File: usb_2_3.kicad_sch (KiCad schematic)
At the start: 0 parts

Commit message: Finished the schematic capture for the USb 2.0/3.0
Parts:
- added C26, C27, C28, C29: 100NF/50V, A_HDJ_Library:C_0402_1005Metric, symbol Device:C_Small
- added C30, C31, C32: 22mF/10V, A_HDJ_Library:C_0603_1608Metric, symbol Device:C
- added D5, D6, D7, D8: ESD9B5.0ST5G, A_HDJ_Library:D_0402_1005Metric, symbol Diode:ESD9B5.0ST5G
- added F2, F3, F4, F5: 6V/1A, A_HDJ_Library:Fuse_0805_2012Metric, symbol Device:Fuse
- added J4: USB3_A_Stacked, A_HDJ_Library:USB3_A_Molex_48406-0001_Horizontal_Stacked, symbol Connector:USB3_A_Stacked
- added J4B: USB3_A_Stacked, symbol Connector:USB3_A_Stacked
- added J5: USB_A_Stacked, A_HDJ_Library:USB_A_CUI_UJ2-ADH-TH_Horizontal_Stacked, symbol Connector:USB_A_Stacked
- added U3, U4, U5: D3V3XA4B10LP, A_HDJ_Library:Diodes_UDFN-10_1.0x2.5mm_P0.5mm, symbol Power_Protection:D3V3XA4B10LP
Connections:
- new net: F3.2, J5.5 (VBUS2)
- new net: F2.2, J5.1 (VBUS1)
- new net: F5.2, J4B.10 (VBUS2)
- new net: F4.2, J4.1 (VBUS1)
- new net +5V: C30.2, C31.2, C32.2, F2.1, F3.1, F4.1, F5.1
- new net CON_USB3_SSTX_N: C26.2, C28.2, J4.8 (SSTX1-), J4B.17 (SSTX2-)
- new net CON_USB3_SSTX_P: C27.2, C29.2, J4.9 (SSTX1+), J4B.18 (SSTX2+)
- new net GND: C30.1, C31.1, C32.1, D5.2 (A2), D6.2 (A2), D7.2 (A2), D8.2 (A2), J4.4 (GND1), J4.7 (DRAIN1), J4.SH (SHIELD), J4B.13 (GND2), J4B.16 (DRAIN2), J4B.SH (SHIELD), J5.4 (GND1), J5.8 (GND2), J5.SH (Shield), U3.3 (VSS), U3.8 (VSS), U4.3 (VSS), U4.8 (VSS), U5.3 (VSS), U5.8 (VSS)
- new net USB3_SSRT_N: C26.1, U3.5, U3.6 (NC)
- new net USB3_SSRT_P: C27.1, U3.4, U3.7 (NC)
- new net USB3_SSRX_N: J4.5 (SSRX1-), J4B.14 (SSRX2-), U5.1, U5.10 (NC), U5.5, U5.6 (NC)
- new net USB3_SSRX_P: J4.6 (SSRX1+), J4B.15 (SSRX2+), U5.2, U5.4, U5.7 (NC), U5.9 (NC)
- new net USB4_SSRT_N: C28.1, U3.1, U3.10 (NC)
- new net USB4_SSRT_P: C29.1, U3.2, U3.9 (NC)
- new net USB_2_P1+: J4.3 (D1+), J4B.12 (D2+)
- new net USB_2_P1-: J4.2 (D1-), J4B.11 (D2-)
- new net USB_2_P3+: D7.1 (A1), J5.7 (D2+), U4.4, U4.7 (NC)
- new net USB_2_P3-: D8.1 (A1), J5.6 (D2-), U4.5, U4.6 (NC)
- new net USB_2_P5+: D5.1 (A1), J5.3 (D1+), U4.1, U4.10 (NC)
- new net USB_2_P5-: D6.1 (A1), J5.2 (D1-), U4.2, U4.9 (NC)

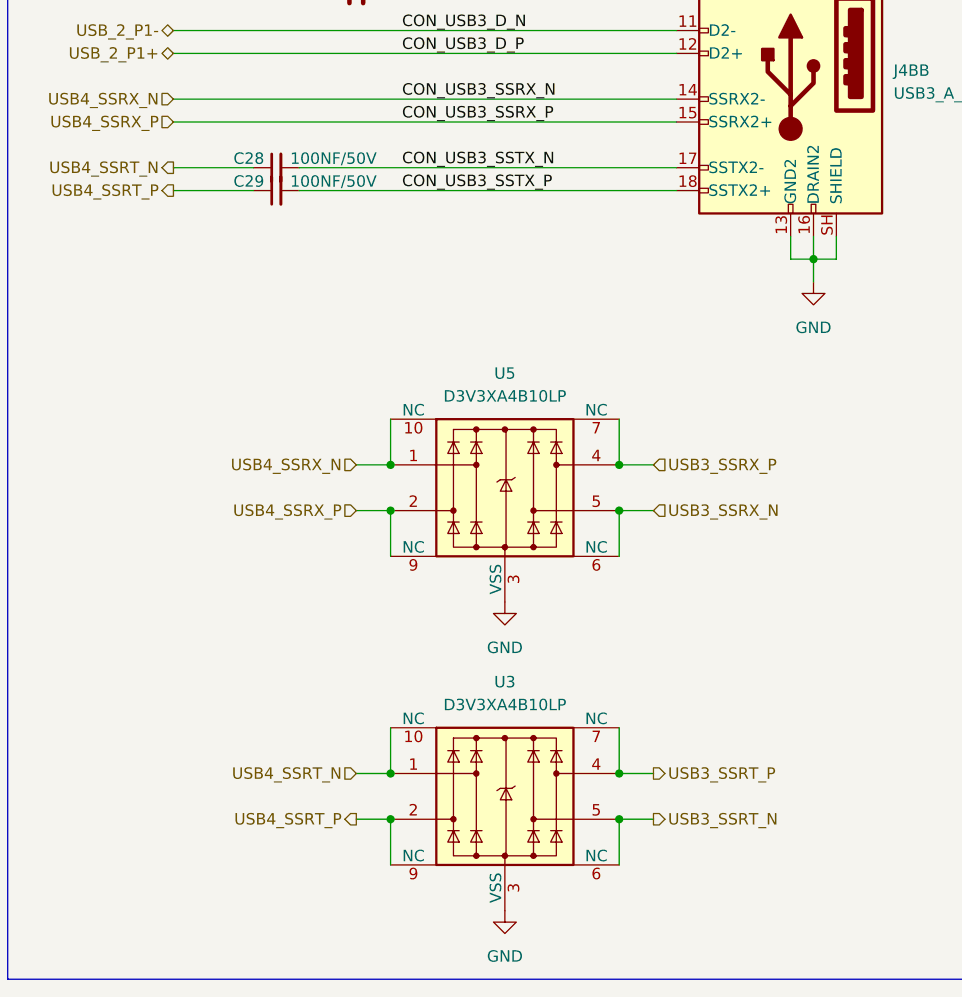
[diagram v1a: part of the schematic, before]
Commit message: Fixed the labels to the netlabels in the USB schema sheet
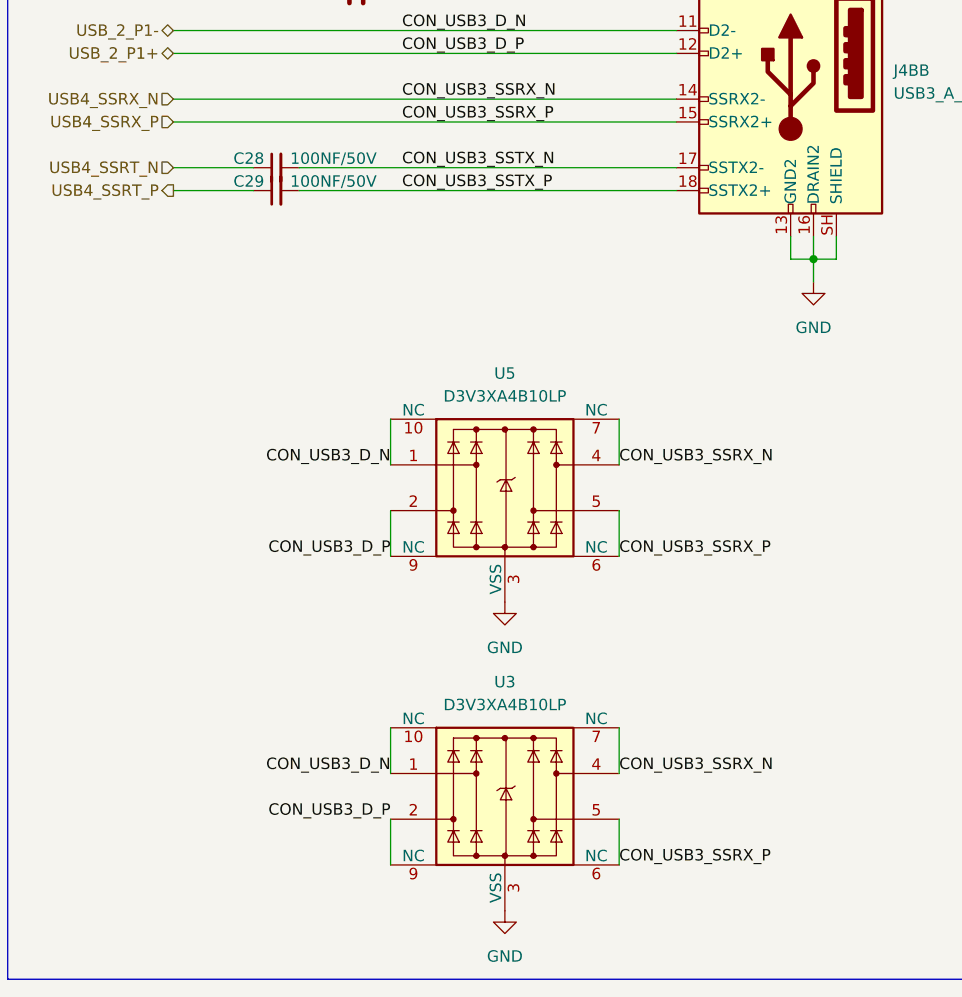
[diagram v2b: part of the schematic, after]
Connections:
- net USB3_SSRT_N: no longer U3.5, U3.6 (NC)
- net USB3_SSRT_P: no longer U3.4, U3.7 (NC)
- net USB3_SSRX_N: now also U3.4, U3.7 (NC), U5.4, U5.7 (NC); no longer U5.1, U5.10 (NC), U5.5, U5.6 (NC)
- net USB3_SSRX_P: now also U3.5, U3.6 (NC), U5.5, U5.6 (NC); no longer U5.2, U5.4, U5.7 (NC), U5.9 (NC)
- net USB4_SSRT_N: no longer U3.1, U3.10 (NC)
- net USB4_SSRT_P: no longer U3.2, U3.9 (NC)
- net USB_2_P1+: now also U3.2, U3.9 (NC), U5.2, U5.9 (NC)
- net USB_2_P1-: now also U3.1, U3.10 (NC), U5.1, U5.10 (NC)
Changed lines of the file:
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@@
-	)
-	(junction
-		(at 55.88 133.35)
-		(diameter 0)
-		(color 0 0 0 0)
-	)
-	(junction
-		(at 55.88 138.43)
-		(diameter 0)
-		(color 0 0 0 0)
-	)
-	(junction
-		(at 81.28 172.72)
-		(diameter 0)
-		(color 0 0 0 0)
 	)
 	(junction
@@
 	)
 	(junction
-		(at 55.88 172.72)
-		(diameter 0)
-		(color 0 0 0 0)
-	)
-	(junction
 		(at 210.82 129.54)
 		(diameter 0)
@@
 	)
 	(junction
-		(at 55.88 167.64)
-		(diameter 0)
-		(color 0 0 0 0)
-	)
-	(junction
-		(at 81.28 133.35)
-		(diameter 0)
-		(color 0 0 0 0)
-	)
-	(junction
 		(at 102.87 59.69)
 		(diameter 0)
 		(color 0 0 0 0)
 	)
-	(junction
-		(at 81.28 138.43)
-		(diameter 0)
-		(color 0 0 0 0)
-	)
-	(junction
-		(at 81.28 167.64)
-		(diameter 0)
-		(color 0 0 0 0)
-	)
 	(wire
 		(pts
@@
 	(wire
 		(pts
-			(xy 81.28 133.35) (xy 85.09 133.35)
-		)
-		(stroke
-			(width 0)
-			(type default)
-		)
-	)
-	(wire
-		(pts
-			(xy 52.07 167.64) (xy 55.88 167.64)
-		)
-		(stroke
-			(width 0)
-			(type default)
-		)
-	)
-	(wire
-		(pts
 			(xy 45.72 102.87) (xy 87.63 102.87)
 		)
@@
 	(wire
 		(pts
-			(xy 81.28 172.72) (xy 85.09 172.72)
-		)
-		(stroke
-			(width 0)
-			(type default)
-		)
-	)
-	(wire
-		(pts
 			(xy 31.75 44.45) (xy 87.63 44.45)
 		)
@@
 	(wire
 		(pts
-			(xy 52.07 138.43) (xy 55.88 138.43)
-		)
-		(stroke
-			(width 0)
-			(type default)
-		)
-	)
-	(wire
-		(pts
 			(xy 194.31 134.62) (xy 210.82 134.62)
 		)
@@
 	(wire
 		(pts
-			(xy 52.07 133.35) (xy 55.88 133.35)
-		)
-		(stroke
-			(width 0)
-			(type default)
-		)
-	)
-	(wire
-		(pts
 			(xy 71.12 29.21) (xy 87.63 29.21)
 		)
@@
 	(wire
 		(pts
-			(xy 52.07 172.72) (xy 55.88 172.72)
-		)
-		(stroke
-			(width 0)
-			(type default)
-		)
-	)
-	(wire
-		(pts
 			(xy 58.42 29.21) (xy 63.5 29.21)
 		)
@@
 	(wire
 		(pts
-			(xy 81.28 167.64) (xy 85.09 167.64)
-		)
-		(stroke
-			(width 0)
-			(type default)
-		)
-	)
-	(wire
-		(pts
 			(xy 45.72 49.53) (xy 87.63 49.53)
 		)
@@
 		(pts
 			(xy 45.72 52.07) (xy 87.63 52.07)
-		)
-		(stroke
-			(width 0)
-			(type default)
-		)
-	)
-	(wire
-		(pts
-			(xy 81.28 138.43) (xy 85.09 138.43)
 		)
 		(stroke
@@
 		)
 	)
+	(label "CON_USB3_D_N"
+		(at 55.88 133.35 180)
+		(effects
+			(font
+				(size 1.27 1.27)
+			)
+			(justify right bottom)
+		)
+	)
+	(label "CON_USB3_D_P"
+		(at 55.88 143.51 180)
+		(effects
+			(font
+				(size 1.27 1.27)
+			)
+			(justify right bottom)
+		)
+	)
 	(label "CON_USB3_SSTX_P"
 		(at 57.15 52.07 0)
@@
 		)
 	)
+	(label "CON_USB3_SSRX_P"
+		(at 81.28 143.51 0)
+		(effects
+			(font
+				(size 1.27 1.27)
+			)
+			(justify left bottom)
+		)
+	)
+	(label "CON_USB3_D_N"
+		(at 55.88 167.64 180)
+		(effects
+			(font
+				(size 1.27 1.27)
+			)
+			(justify right bottom)
+		)
+	)
 	(label "CON_USB3_D_N"
 		(at 57.15 34.29 0)
@@
 		)
 	)
+	(label "CON_USB3_SSRX_N"
+		(at 81.28 167.64 0)
+		(effects
+			(font
+				(size 1.27 1.27)
+			)
+			(justify left bottom)
+		)
+	)
 	(label "CON_USB2_D_N"
 		(at 207.01 81.28 0)
@@
 		)
 	)
+	(label "CON_USB3_SSRX_N"
+		(at 81.28 133.35 0)
+		(effects
+			(font
+				(size 1.27 1.27)
+			)
+			(justify left bottom)
+		)
+	)
 	(label "CON_USB1_D_P"
 		(at 170.18 119.38 180)
@@
 		)
 	)
+	(label "CON_USB3_SSRX_P"
+		(at 81.28 177.8 0)
+		(effects
+			(font
+				(size 1.27 1.27)
+			)
+			(justify left bottom)
+		)
+	)
 	(label "CON_USB2_D_N"
 		(at 185.42 55.88 0)
@@
 		)
 	)
+	(label "CON_USB3_D_P"
+		(at 55.88 172.72 180)
+		(effects
+			(font
+				(size 1.27 1.27)
+			)
+			(justify right bottom)
+		)
+	)
 	(label "CON_USB1_D_P"
 		(at 185.42 48.26 0)
@@
 			)
 			(justify left bottom)
-		)
-	)
-	(hierarchical_label "USB3_SSRT_P"
-		(shape output)
-		(at 85.09 167.64 0)
-		(effects
-			(font
-				(size 1.27 1.27)
-			)
-			(justify left)
-		)
-	)
-	(hierarchical_label "USB3_SSRX_P"
-		(shape input)
-		(at 85.09 133.35 0)
-		(effects
-			(font
-				(size 1.27 1.27)
-			)
-			(justify left)
-		)
-	)
-	(hierarchical_label "USB4_SSRT_P"
-		(shape output)
-		(at 52.07 172.72 180)
-		(effects
-			(font
-				(size 1.27 1.27)
-			)
-			(justify right)
 		)
 	)
@@
 	)
 	(hierarchical_label "USB4_SSRT_N"
-		(shape output)
+		(shape input)
 		(at 31.75 100.33 180)
 		(effects
@@
 			)
 			(justify right)
-		)
-	)
-	(hierarchical_label "USB3_SSRX_N"
-		(shape input)
-		(at 85.09 138.43 0)
-		(effects
-			(font
-				(size 1.27 1.27)
-			)
-			(justify left)
 		)
 	)
@@
 		)
 	)
-	(hierarchical_label "USB4_SSRT_N"
-		(shape input)
-		(at 52.07 167.64 180)
-		(effects
-			(font
-				(size 1.27 1.27)
-			)
-			(justify right)
-		)
-	)
-	(hierarchical_label "USB4_SSRX_N"
-		(shape input)
-		(at 52.07 133.35 180)
-		(effects
-			(font
-				(size 1.27 1.27)
-			)
-			(justify right)
-		)
-	)
 	(hierarchical_label "USB_2_P5-"
 		(shape bidirectional)
@@
 		)
 	)
-	(hierarchical_label "USB4_SSRX_P"
-		(shape input)
-		(at 52.07 138.43 180)
-		(effects
-			(font
-				(size 1.27 1.27)
-			)
-			(justify right)
-		)
-	)
 	(hierarchical_label "USB3_SSRT_N"
 		(shape output)
@@
 		)
 	)
-	(hierarchical_label "USB3_SSRT_N"
-		(shape output)
-		(at 85.09 172.72 0)
-		(effects
-			(font
-				(size 1.27 1.27)
-			)
-			(justify left)
-		)
-	)

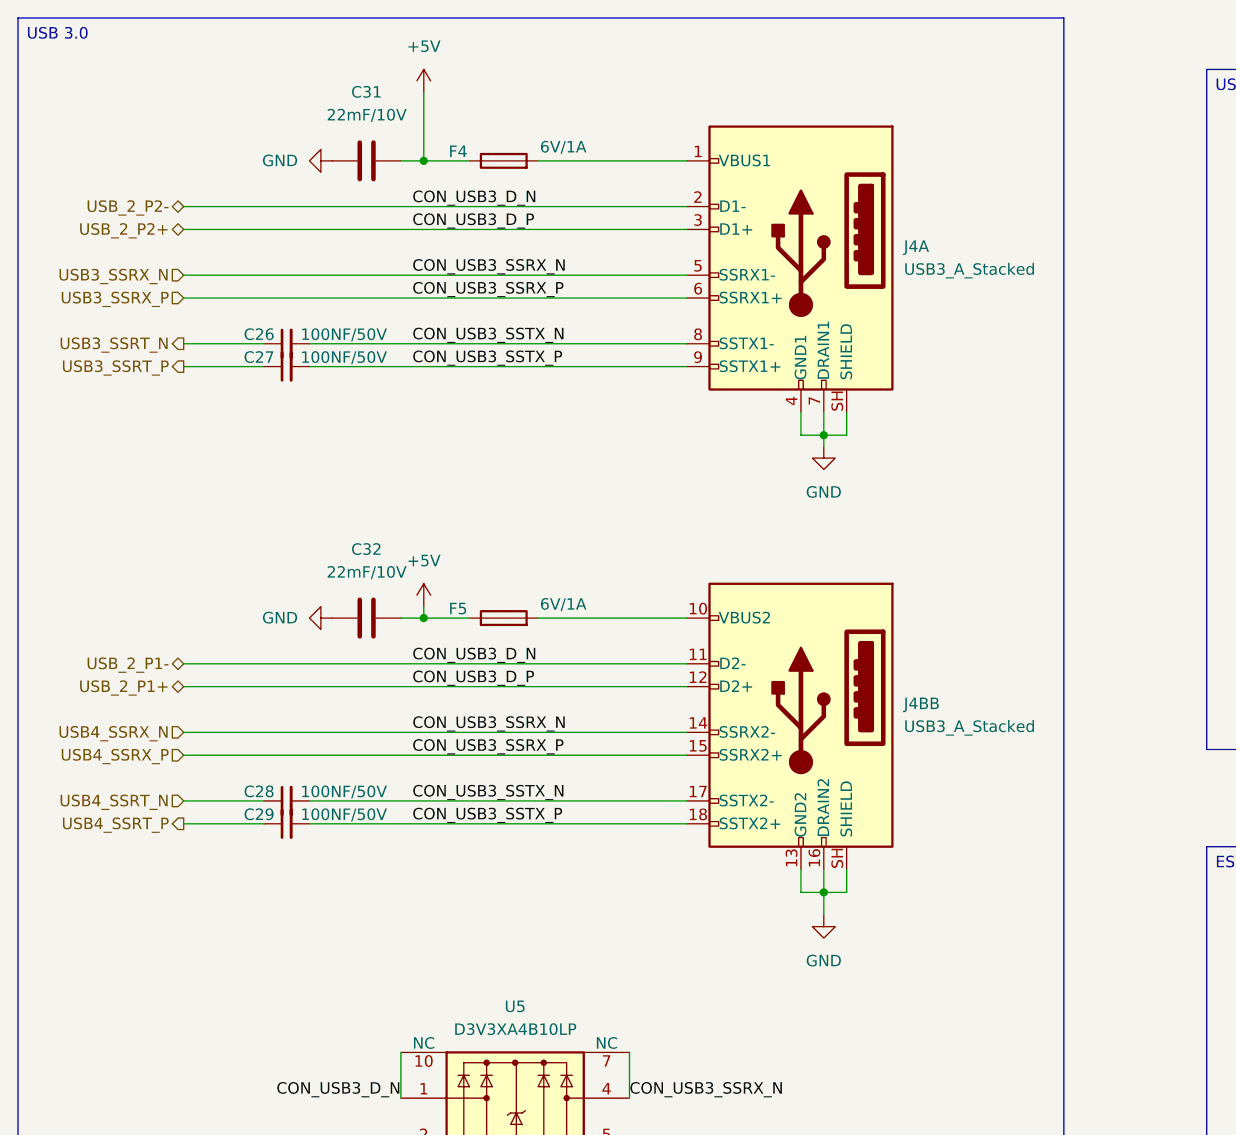
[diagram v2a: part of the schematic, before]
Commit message: Connected the usb sheets together in the the roor sheet
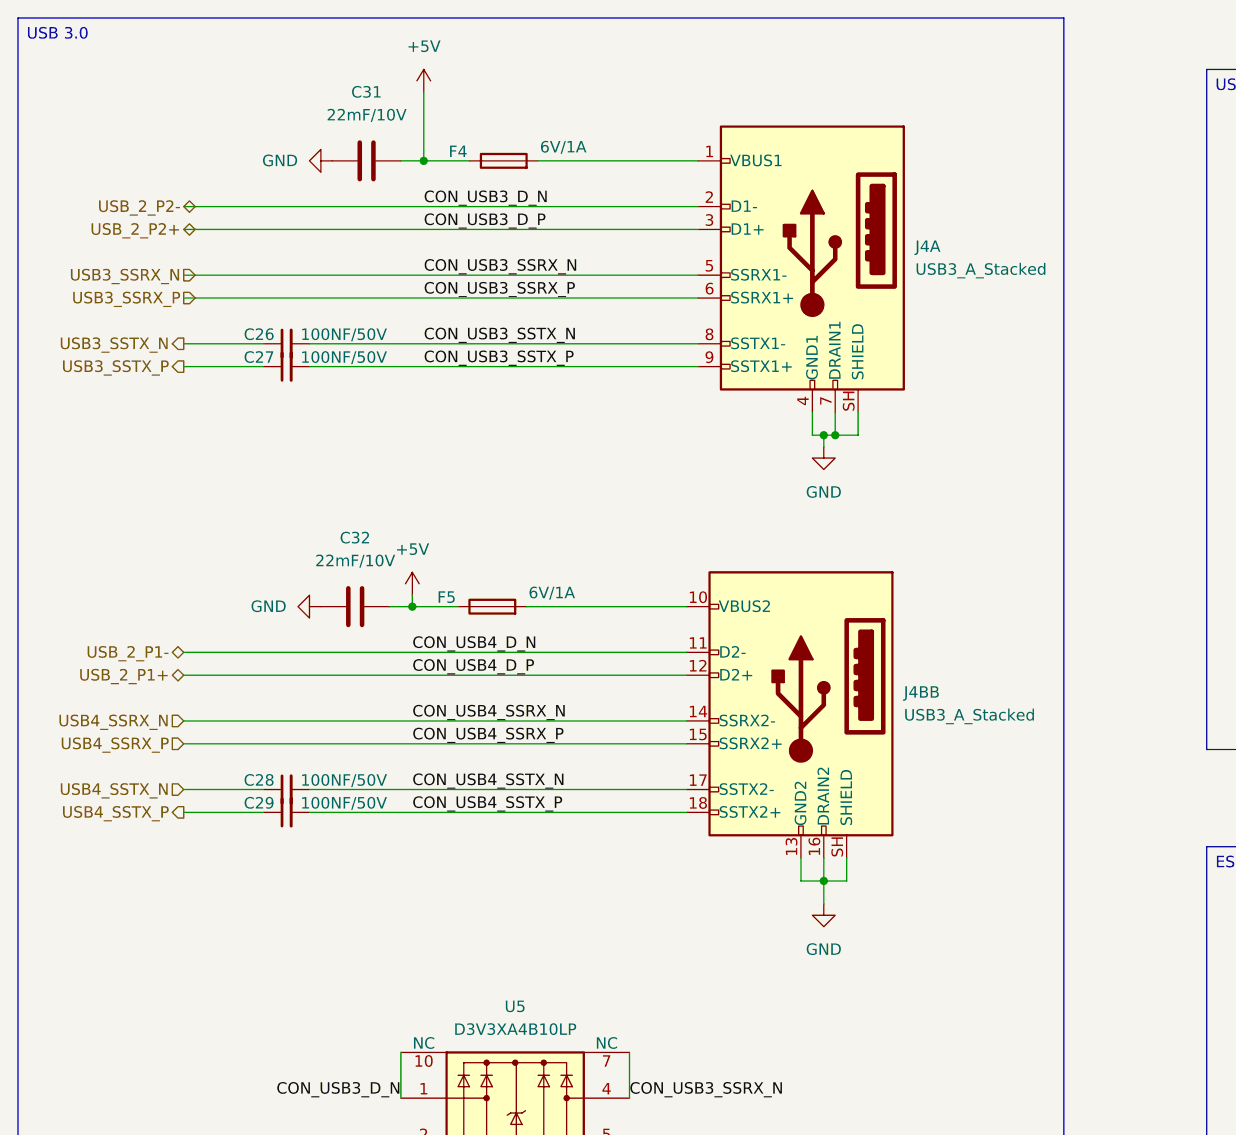
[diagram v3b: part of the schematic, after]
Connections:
- net CON_USB3_SSTX_N: no longer C28.2, J4B.17 (SSTX2-)
- net CON_USB3_SSTX_P: no longer C29.2, J4B.18 (SSTX2+)
- net USB3_SSRX_N: no longer J4B.14 (SSRX2-)
- net USB3_SSRX_P: no longer J4B.15 (SSRX2+)
- net USB_2_P1+: no longer J4.3 (D1+), U3.2, U3.9 (NC), U5.2, U5.9 (NC)
- net USB_2_P1-: no longer J4.2 (D1-), U3.1, U3.10 (NC), U5.1, U5.10 (NC)
- net USB3_SSRT_N renamed USB3_SSTX_N
- net USB3_SSRT_P renamed USB3_SSTX_P
- net USB4_SSRT_N renamed USB4_SSTX_N
- net USB4_SSRT_P renamed USB4_SSTX_P
- new net CON_USB4_SSTX_N: C28.2, J4B.17 (SSTX2-)
- new net CON_USB4_SSTX_P: C29.2, J4B.18 (SSTX2+)
- new net USB4_SSRX_N: J4B.14 (SSRX2-)
- new net USB4_SSRX_P: J4B.15 (SSRX2+)
- new net USB_2_P2+: J4.3 (D1+), U3.2, U3.9 (NC), U5.2, U5.9 (NC)
- new net USB_2_P2-: J4.2 (D1-), U3.1, U3.10 (NC), U5.1, U5.10 (NC)
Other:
- moved on the sheet: C28, C29, C32, F5, J4A, J4BB

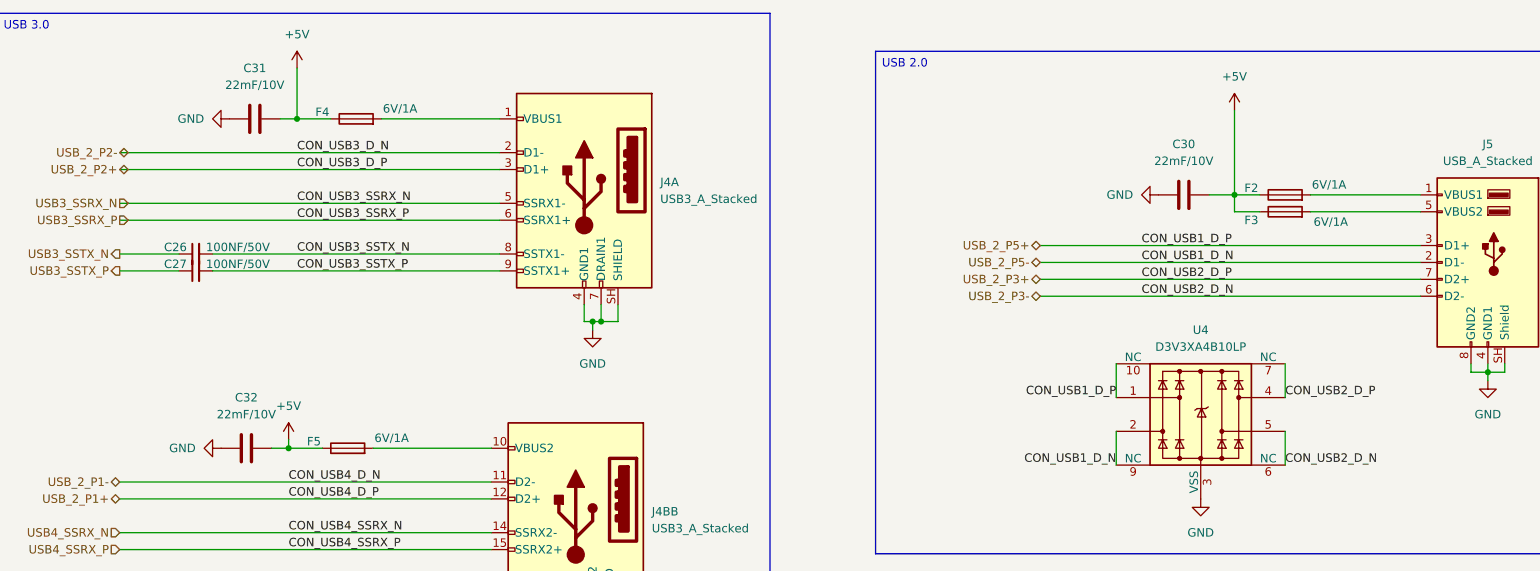
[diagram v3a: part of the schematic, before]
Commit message: Fixed the erc power fleag erro in the USB sub sheet
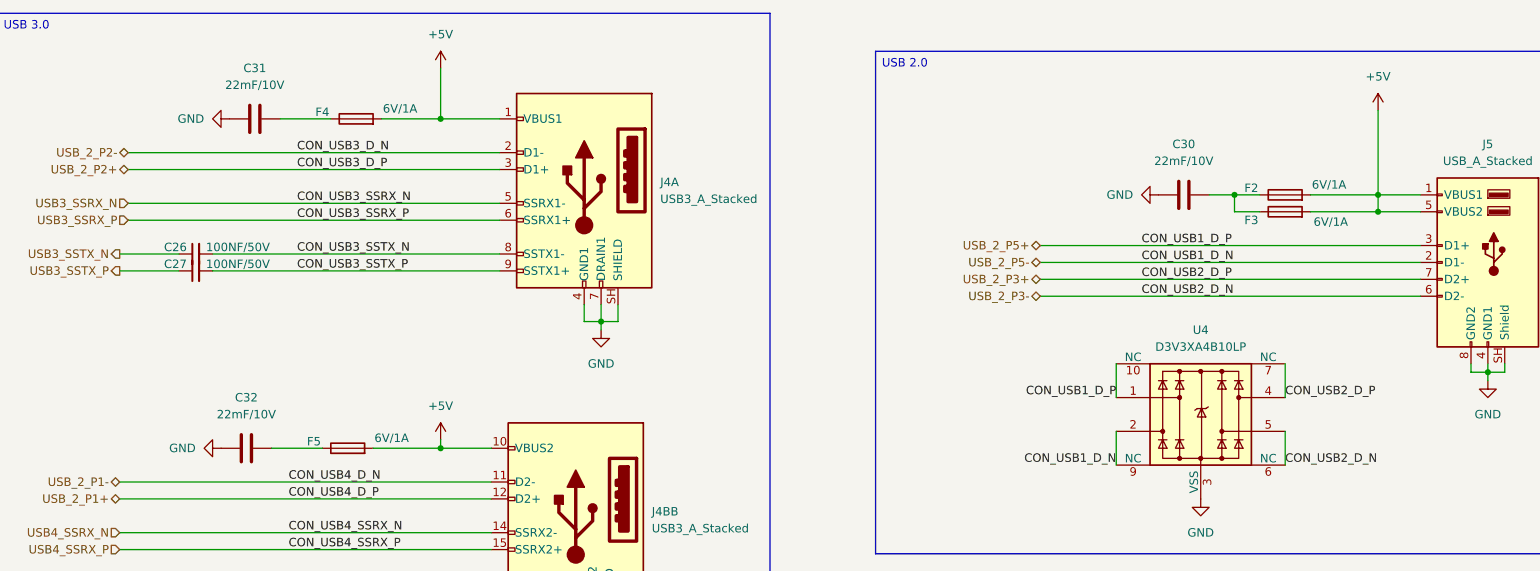
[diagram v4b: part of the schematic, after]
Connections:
- net +5V: now also F2.2, F3.2, F4.2, F5.2, J4.1 (VBUS1), J4B.10 (VBUS2), J5.1 (VBUS1), J5.5 (VBUS2); no longer C30.2, C31.2, C32.2, F2.1, F3.1, F4.1, F5.1
- new net: C30.2, F2.1, F3.1
- new net: C32.2, F5.1
- new net: C31.2, F4.1
